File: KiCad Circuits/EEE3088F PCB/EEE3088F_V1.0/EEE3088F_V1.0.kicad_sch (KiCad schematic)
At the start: 0 parts

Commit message: 2x16 connector added
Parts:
- added J1: Conn_02x16_Odd_Even, symbol Connector_Generic:Conn_02x16_Odd_Even
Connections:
- new net CTRL_EXT_LOAD1: J1.25 (Pin_25)
- new net CTRL_EXT_LOAD2: J1.7 (Pin_7)
- new net EXT_LOAD1_OUT: J1.21 (Pin_21)
- new net EXT_LOAD2_OUT: J1.11 (Pin_11)
- new net GND: J1.19 (Pin_19), J1.23 (Pin_23)
- new net MOTOR1_A_OUT: J1.32 (Pin_32)
- new net MOTOR1_B_OUT: J1.31 (Pin_31)
- new net MOTOR1_CTRL1: J1.28 (Pin_28)
- new net MOTOR1_CTRL2: J1.30 (Pin_30)
- new net MOTOR2_A_OUT: J1.2 (Pin_2)
- new net MOTOR2_B_OUT: J1.1 (Pin_1)
- new net MOTOR2_CTRL1: J1.4 (Pin_4)
- new net MOTOR2_CTRL2: J1.6 (Pin_6)
- new net MOTOR3_A_OUT: J1.27 (Pin_27)
- new net MOTOR3_B_OUT: J1.29 (Pin_29)
- new net MOTOR3_CTRL1: J1.24 (Pin_24)
- new net MOTOR3_CTRL2: J1.26 (Pin_26)
- new net MOTOR4_A_OUT: J1.3 (Pin_3)
- new net MOTOR4_B_OUT: J1.5 (Pin_5)
- new net MOTOR4_CTRL1: J1.8 (Pin_8)
- new net MOTOR4_CTRL2: J1.10 (Pin_10)

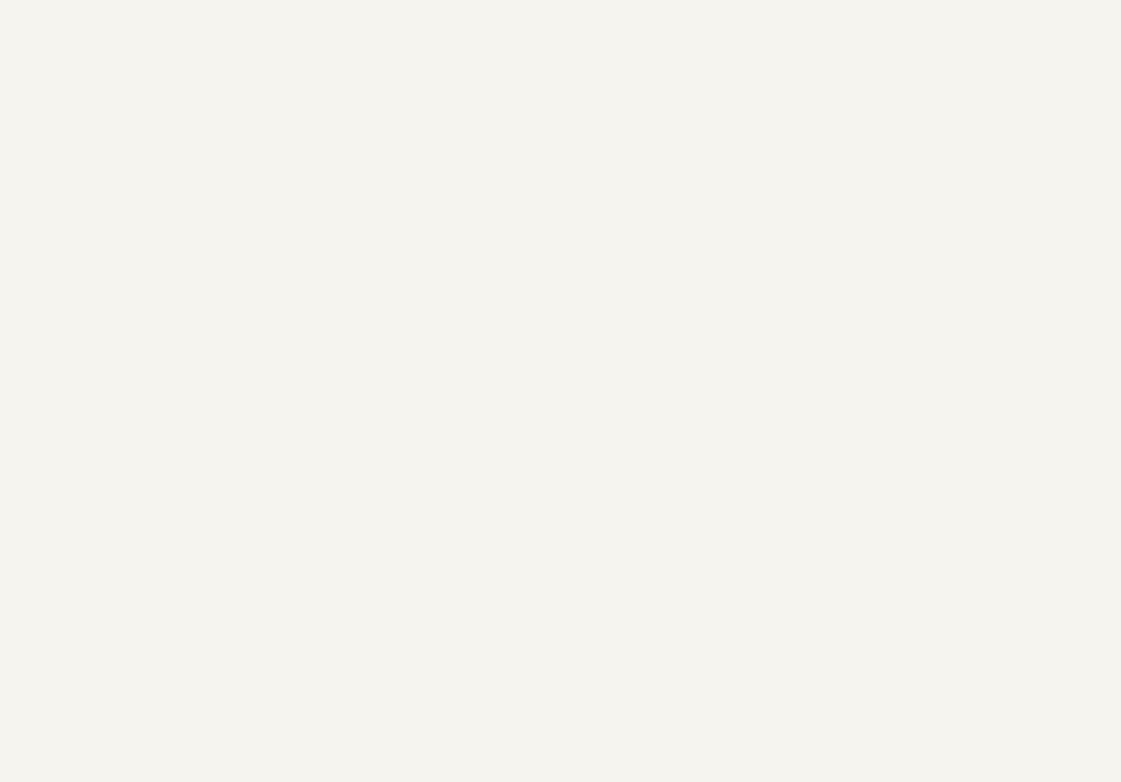
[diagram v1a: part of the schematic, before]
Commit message: Added 1 H-bridge (DRV8833PWP)
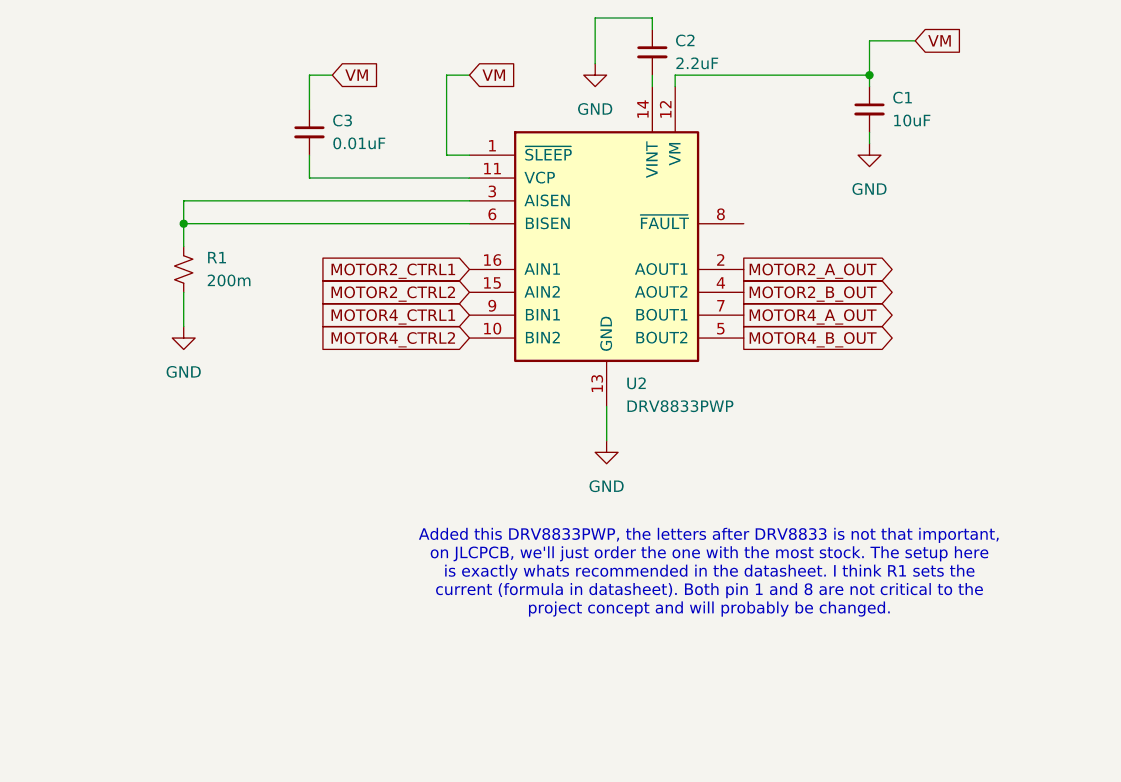
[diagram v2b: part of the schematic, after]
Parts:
- added C1: 10uF, symbol Device:C_Small
- added C2: 2.2uF, symbol Device:C_Small
- added C3: 0.01uF, symbol Device:C_Small
- added R1: 200m, symbol Device:R_Small_US
- added U2: DRV8833PWP, Package_SO:HTSSOP-16-1EP_4.4x5mm_P0.65mm_EP3.4x5mm_Mask2.46x2.31mm_ThermalVias, symbol Driver_Motor:DRV8833PWP
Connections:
- net GND: now also C1.2, C2.1, R1.2, U2.13 (GND), U2.17 (GND)
- net MOTOR2_A_OUT: now also U2.2 (AOUT1)
- net MOTOR2_B_OUT: now also U2.4 (AOUT2)
- net MOTOR2_CTRL1: now also U2.16 (AIN1)
- net MOTOR2_CTRL2: now also U2.15 (AIN2)
- net MOTOR4_A_OUT: now also U2.7 (BOUT1)
- net MOTOR4_B_OUT: now also U2.5 (BOUT2)
- net MOTOR4_CTRL1: now also U2.9 (BIN1)
- net MOTOR4_CTRL2: now also U2.10 (BIN2)
- new net: C3.2, U2.11 (VCP)
- new net: C2.2, U2.14 (VINT)
- new net: R1.1, U2.3 (AISEN), U2.6 (BISEN)
- new net VM: C1.1, C3.1, U2.1 (~{SLEEP}), U2.12 (VM)
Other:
- note added: "Added this DRV8833PWP, the letters after DRV8833 is not that important, on JLCPCB, we'll just order the one with the most stock. The setup here is exactly whats recommended in the datasheet. I think R1 sets the current (formula in datasheet). Both pin 1 and 8 are not critical to the project concept and will probably be changed."

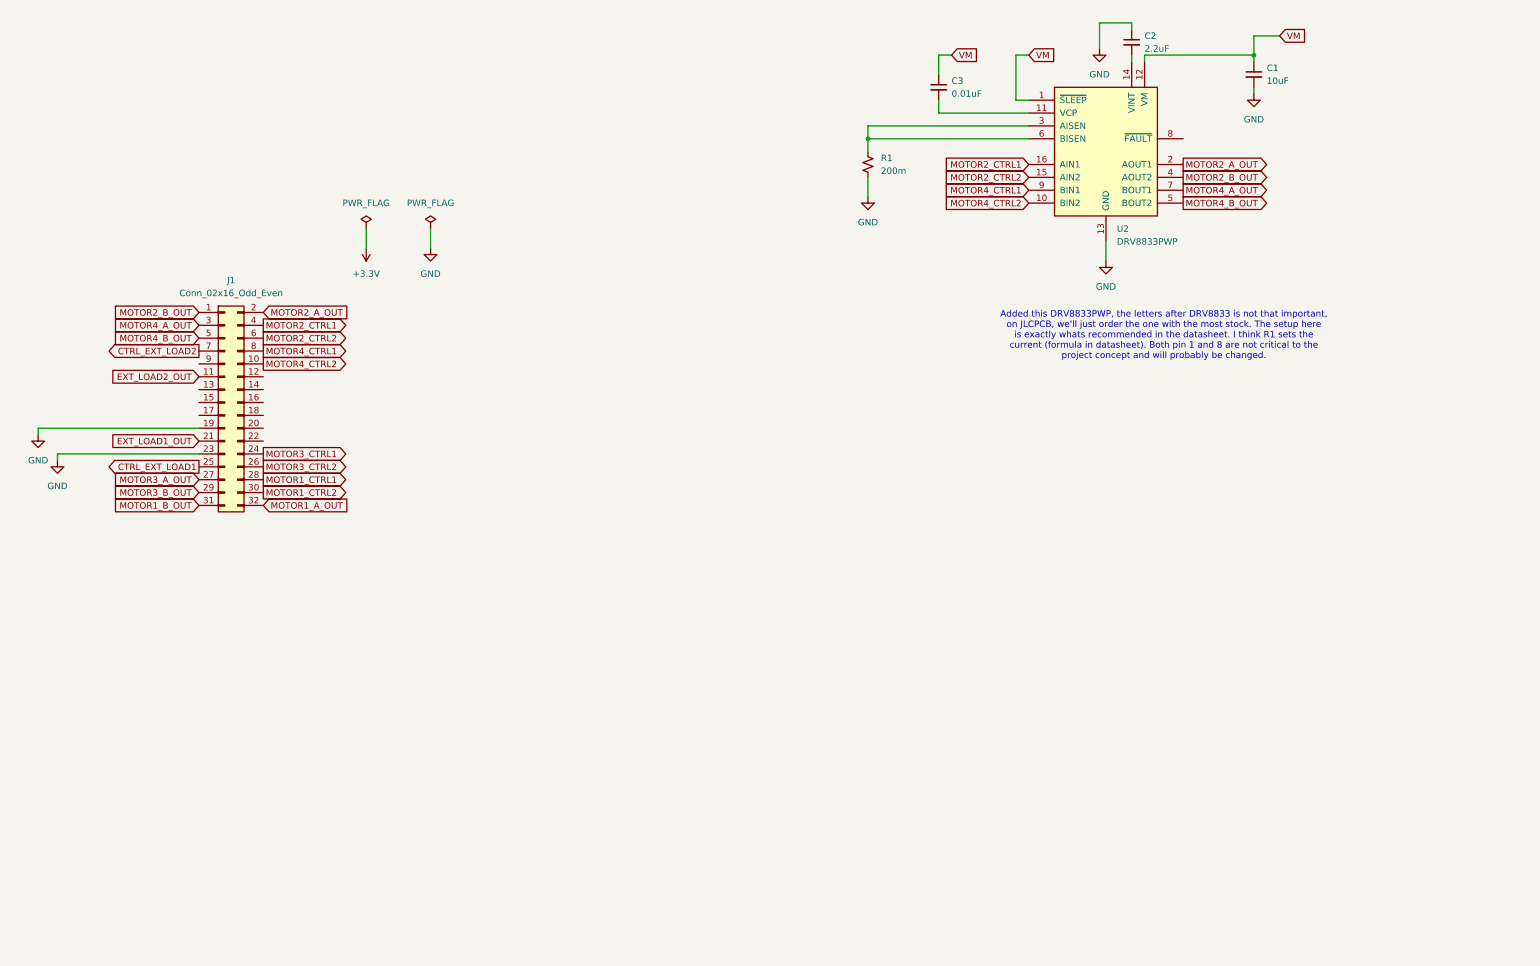
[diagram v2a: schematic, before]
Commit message: Added H-bridge and voltage regulators
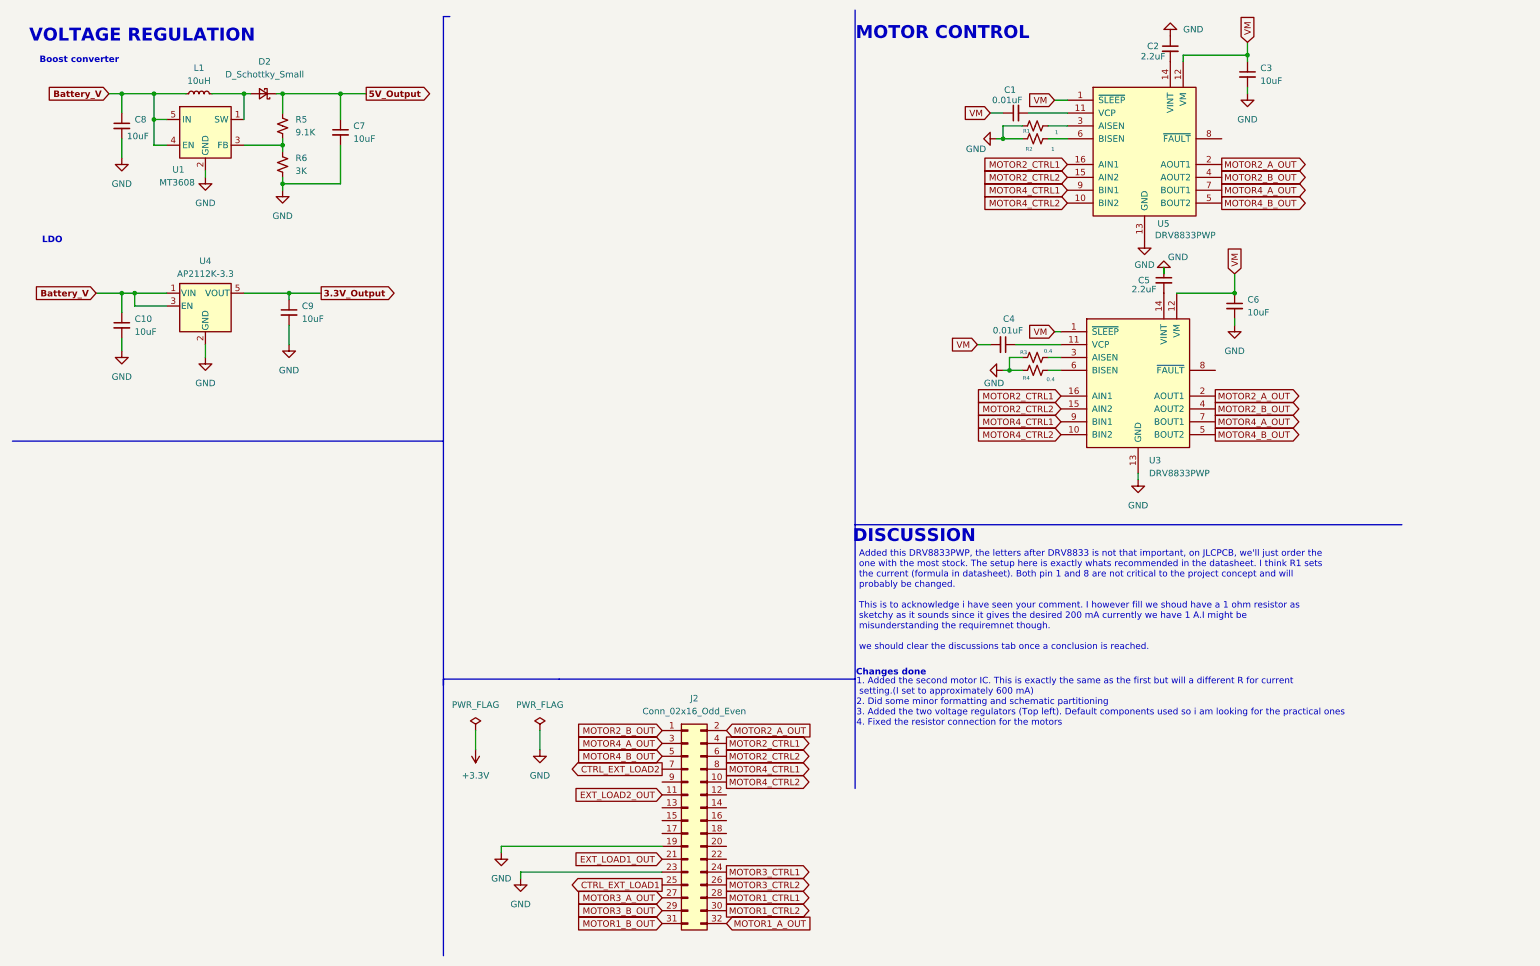
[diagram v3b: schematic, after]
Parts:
- removed J1: Conn_02x16_Odd_Even, symbol Connector_Generic:Conn_02x16_Odd_Even
- removed U2: DRV8833PWP, Package_SO:HTSSOP-16-1EP_4.4x5mm_P0.65mm_EP3.4x5mm_Mask2.46x2.31mm_ThermalVias, symbol Driver_Motor:DRV8833PWP
- added C10, C6, C7, C8, C9: 10uF, symbol Device:C_Small
- added C4: 0.01uF, symbol Device:C_Small
- added C5: 2.2uF, symbol Device:C_Small
- added D2: D_Schottky_Small, symbol Device:D_Schottky_Small
- added J2: Conn_02x16_Odd_Even, symbol Connector_Generic:Conn_02x16_Odd_Even
- added L1: 10uH, symbol Device:L_Small
- added R2: 1, symbol Device:R_Small_US
- added R3, R4: 0.4, symbol Device:R_Small_US
- added R5: 9.1K, symbol Device:R_Small_US
- added R6: 3K, symbol Device:R_Small_US
- added U1: MT3608, Package_TO_SOT_SMD:SOT-23-6, symbol Regulator_Switching:MT3608
- added U3, U5: DRV8833PWP, Package_SO:HTSSOP-16-1EP_4.4x5mm_P0.65mm_EP3.4x5mm_Mask2.46x2.31mm_ThermalVias, symbol Driver_Motor:DRV8833PWP
- added U4: AP2112K-3.3, Package_TO_SOT_SMD:SOT-23-5, symbol Regulator_Linear:AP2112K-3.3
- C1: value 10uF -> 0.01uF
- C3: value 0.01uF -> 10uF
- R1: value 200m -> 1
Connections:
- net CTRL_EXT_LOAD1: now also J2.25 (Pin_25)
- net CTRL_EXT_LOAD2: now also J2.7 (Pin_7)
- net EXT_LOAD1_OUT: now also J2.21 (Pin_21)
- net EXT_LOAD2_OUT: now also J2.11 (Pin_11)
- net GND: now also C3.2, R1.1, C10.2, C5.1, C6.2, C7.2, C8.2, C9.2, J2.19 (Pin_19), J2.23 (Pin_23), R2.1, R3.1, R4.1, R6.2, U1.2 (GND), U3.13 (GND), U3.17 (GND), U4.2 (GND), U5.13 (GND), U5.17 (GND); no longer C1.2, R1.2
- net MOTOR1_A_OUT: now also J2.32 (Pin_32)
- net MOTOR1_B_OUT: now also J2.31 (Pin_31)
- net MOTOR1_CTRL1: now also J2.28 (Pin_28)
- net MOTOR1_CTRL2: now also J2.30 (Pin_30)
- net MOTOR2_A_OUT: now also J2.2 (Pin_2), U3.2 (AOUT1), U5.2 (AOUT1)
- net MOTOR2_B_OUT: now also J2.1 (Pin_1), U3.4 (AOUT2), U5.4 (AOUT2)
- net MOTOR2_CTRL1: now also J2.4 (Pin_4), U3.16 (AIN1), U5.16 (AIN1)
- net MOTOR2_CTRL2: now also J2.6 (Pin_6), U3.15 (AIN2), U5.15 (AIN2)
- net MOTOR3_A_OUT: now also J2.27 (Pin_27)
- net MOTOR3_B_OUT: now also J2.29 (Pin_29)
- net MOTOR3_CTRL1: now also J2.24 (Pin_24)
- net MOTOR3_CTRL2: now also J2.26 (Pin_26)
- net MOTOR4_A_OUT: now also J2.3 (Pin_3), U3.7 (BOUT1), U5.7 (BOUT1)
- net MOTOR4_B_OUT: now also J2.5 (Pin_5), U3.5 (BOUT2), U5.5 (BOUT2)
- net MOTOR4_CTRL1: now also J2.8 (Pin_8), U3.9 (BIN1), U5.9 (BIN1)
- net MOTOR4_CTRL2: now also J2.10 (Pin_10), U3.10 (BIN2), U5.10 (BIN2)
- net VM: now also C4.2, C6.1, U3.1 (~{SLEEP}), U3.12 (VM), U5.1 (~{SLEEP}), U5.12 (VM)
- net at C2.2: now also U5.14 (VINT)
- new net: C4.1, U3.11 (VCP)
- new net: C5.2, U3.14 (VINT)
- new net: R3.2, U3.3 (AISEN)
- new net: R4.2, U3.6 (BISEN)
- new net: C1.2, U5.11 (VCP)
- new net: D2.2 (A), L1.2, U1.1 (SW)
- new net: R2.2, U5.6 (BISEN)
- new net: R1.2, U5.3 (AISEN)
- new net: R5.2, R6.1, U1.3 (FB)
- new net 3.3V_Output: C9.1, U4.5 (VOUT)
- new net 5V_Output: C7.1, D2.1 (K), R5.1
- new net Battery_V: C10.1, C8.1, L1.1, U1.4 (EN), U1.5 (IN), U4.1 (VIN), U4.3 (EN)
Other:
- note added: "1. Added the second motor IC. This is exactly the same as the first but will a different R for current setting.(I set to approximately 600 mA) 2. Did some minor formatting and schematic partitioning 3. Added the two voltage regulators (Top left). Default components used so i am looking for the practical ones 4. Fixed the resistor connection for the motors"
- note added: "Added this DRV8833PWP, the letters after DRV8833 is not that important, on JLCPCB, we'll just order the one with the most stock. The setup here is exactly whats recommended in the datasheet. I think R1 sets the current (formula in datasheet). Both pin 1 and 8 are not critical to the project concept and will probably be changed. This is to acknowledge i have seen your comment. I however fill we sh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"
- note added: "Boost converter"
- note added: "Changes done"
- note added: "DISCUSSION"
- note added: "LDO"
- note added: "MOTOR CONTROL"
- note added: "VOLTAGE REGULATION"
- note removed: "Added this DRV8833PWP, the letters after DRV8833 is not that important, on JLCPCB, we'll just order the one with the most stock. The setup here is exactly whats recommended in the datasheet. I think R1 sets the current (formula in datasheet). Both pin 1 and 8 are not critical to the project concept and will probably be changed."

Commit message: Added INA219 and did housekeeping
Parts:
- added J1: Conn_01x02_Pin, symbol Connector:Conn_01x02_Pin
- added U2: INA219AxD, Package_SO:SOIC-8_3.9x4.9mm_P1.27mm, symbol Sensor_Energy:INA219AxD
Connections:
- net VM is gone; now on net Battery_V: C1.1, C3.1, C4.2, C6.1, U3.1 (~{SLEEP}), U3.12 (VM), U5.1 (~{SLEEP}), U5.12 (VM)
- net Battery_V: now also J1.1 (Pin_1), U2.8 (IN+)
- net GND: now also J1.2 (Pin_2), U2.6 (GND), U2.7 (IN-)
- net MOTOR1_A_OUT: now also U3.2 (AOUT1)
- net MOTOR1_B_OUT: now also U3.4 (AOUT2)
- net MOTOR1_CTRL1: now also U3.16 (AIN1)
- net MOTOR1_CTRL2: now also U3.15 (AIN2)
- net MOTOR2_A_OUT: no longer U3.2 (AOUT1)
- net MOTOR2_B_OUT: no longer U3.4 (AOUT2)
- net MOTOR2_CTRL1: no longer U3.16 (AIN1)
- net MOTOR2_CTRL2: no longer U3.15 (AIN2)
- net MOTOR3_A_OUT: now also U3.7 (BOUT1)
- net MOTOR3_B_OUT: now also U3.5 (BOUT2)
- net MOTOR3_CTRL1: now also U3.9 (BIN1)
- net MOTOR3_CTRL2: now also U3.10 (BIN2)
- net MOTOR4_A_OUT: no longer U3.7 (BOUT1)
- net MOTOR4_B_OUT: no longer U3.5 (BOUT2)
- net MOTOR4_CTRL1: no longer U3.9 (BIN1)
- net MOTOR4_CTRL2: no longer U3.10 (BIN2)
- net FAST_CHARGE_CTRL: now reaches J2.13 (Pin_13)
- net I2C1_SCL: now reaches J2.16 (Pin_16)
- net I2C1_SCL: now also U2.4 (SCL)
- net I2C1_SDA: now reaches J2.17 (Pin_17)
- net I2C1_SDA: now also U2.3 (SDA)
- net 3V3 Out: now reaches J2.18 (Pin_18)
- net 5V Out: now reaches J2.20 (Pin_20)
- net HV: now reaches J2.22 (Pin_22)
- net 3.3V_Output renamed 3.3V_Out
- net 5V_Output renamed 5V_Out
- net 5V_Out: now also U2.5 (VS)
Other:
- note added: "Changed the motor labels, all motors now included. Changed the VM label for each IC, and linked VM to the battery voltage. Added the INA219, and connected most pins."
- note added: "INA219 and JST Connector"
- note added: "Input voltage VM is the Battery voltage"
- moved on the sheet: C1, C2, C3, C4, C5, C6, R1, R2, R3, R4, U3, U5
